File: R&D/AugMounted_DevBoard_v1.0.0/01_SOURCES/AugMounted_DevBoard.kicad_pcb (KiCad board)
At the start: 2 copper layers, 56.8 x 89.5 mm, 140 parts, among them J201 J_TYPE-C-31-M-13, J301 J_JST_S2B-PH-SM4-TB, J401 J_FH43BW-61S-0.2SHW, J501 J_0788641001_PAD, J502 J_0788641001, J503 J_0788641001, J504 J_0788641001_PAD, Q301 Q_BSS123WQ-7-F, Q302 Q_HSS2P10, Q303 Q_BSS123WQ-7-F, Q304 Q_BSS123WQ-7-F, Q305 Q_HSS2P10, Q401 Q_BSS123WQ-7-F, Q501 Q_BSS123WQ-7-F, SW501 SW_SKRTLAE010, SW601 SW_EC12D1564404, SW602 SW_SKRTLAE010, SW603 SW_SKRTLAE010, U201 ESP32-S3-WROOM-1U-N16R8, U202 U_MCP23017T-E/ML, U301 U_LP3987H-18B5F, U302 U_MAX17048G+T10, U303 U_BQ24296MRGER, U304 U_TPS63001DRCR, U305 U_TPS61087DRCR, U401 U_TXB0108PWR, U402 U_TXB0108PWR, U403 U_TXB0108PWR, U501 U_VCNL4040M3OE, U502 ICS‐41350, U503 LIS2DW12

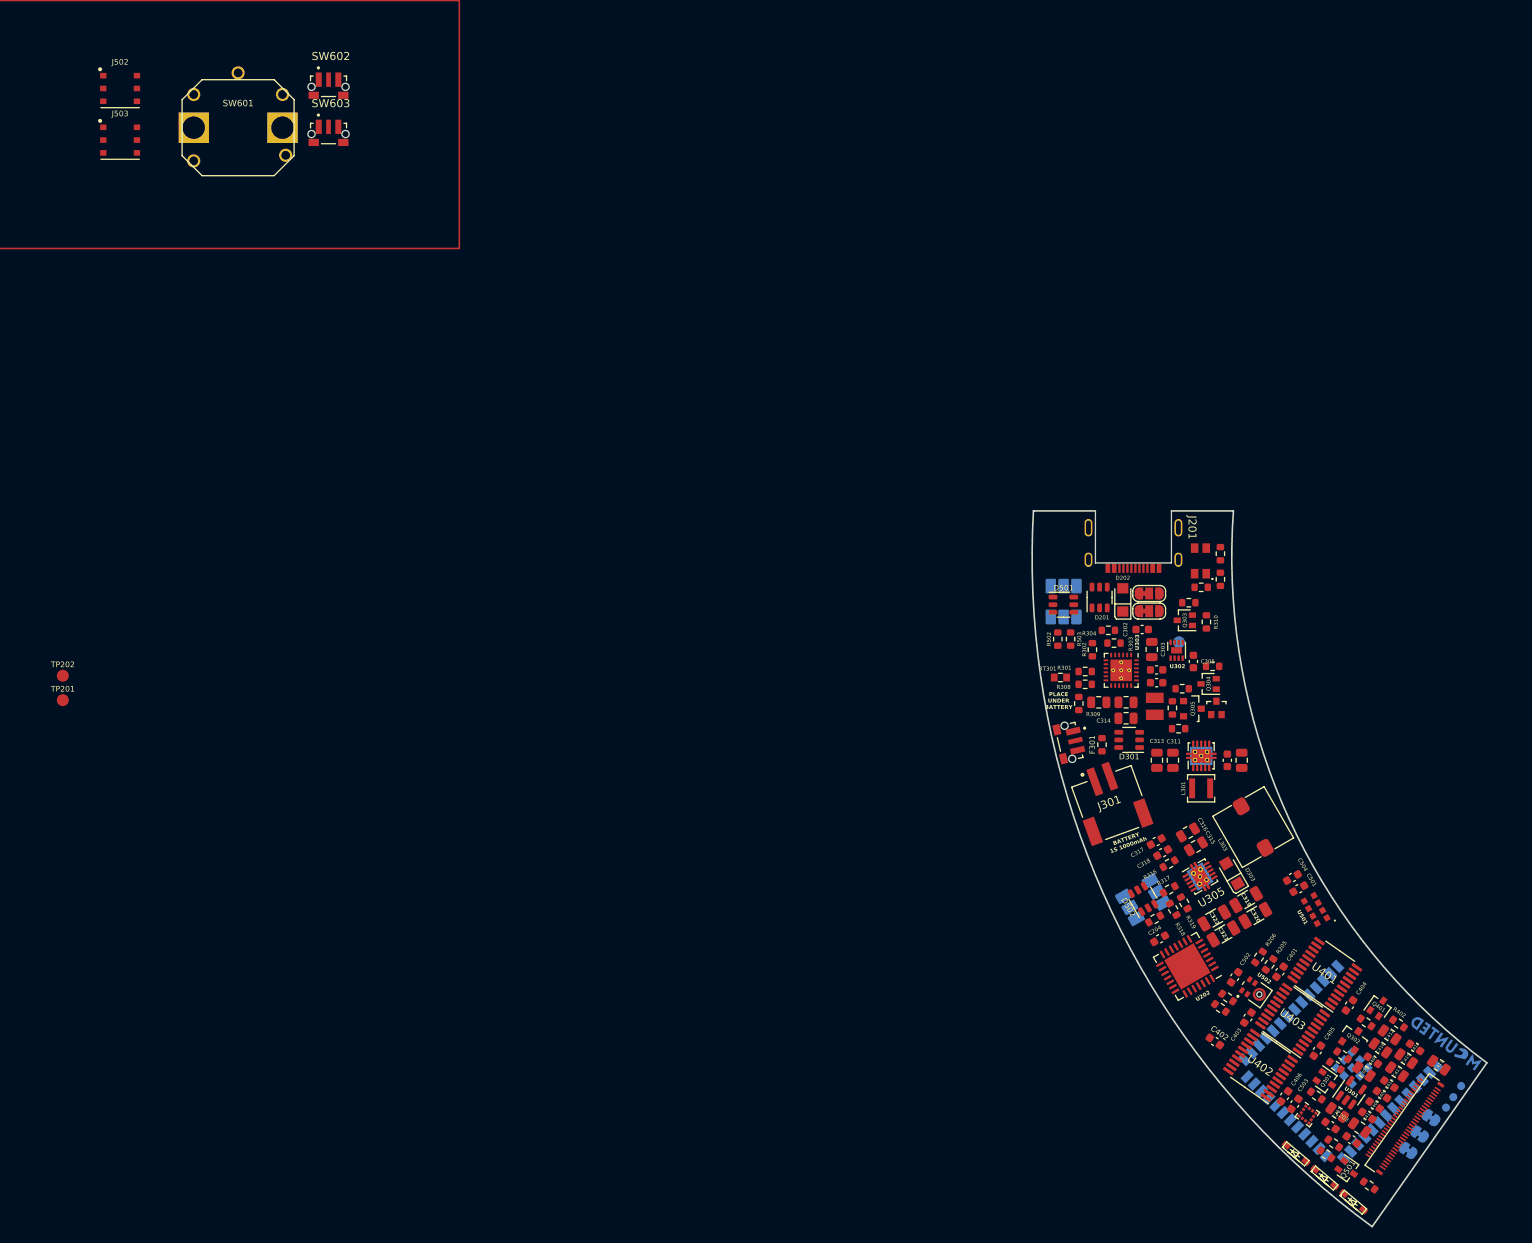
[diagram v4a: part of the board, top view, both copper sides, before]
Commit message: Added resistors for CC1 and CC2 pins, layout is started on the high part of the board
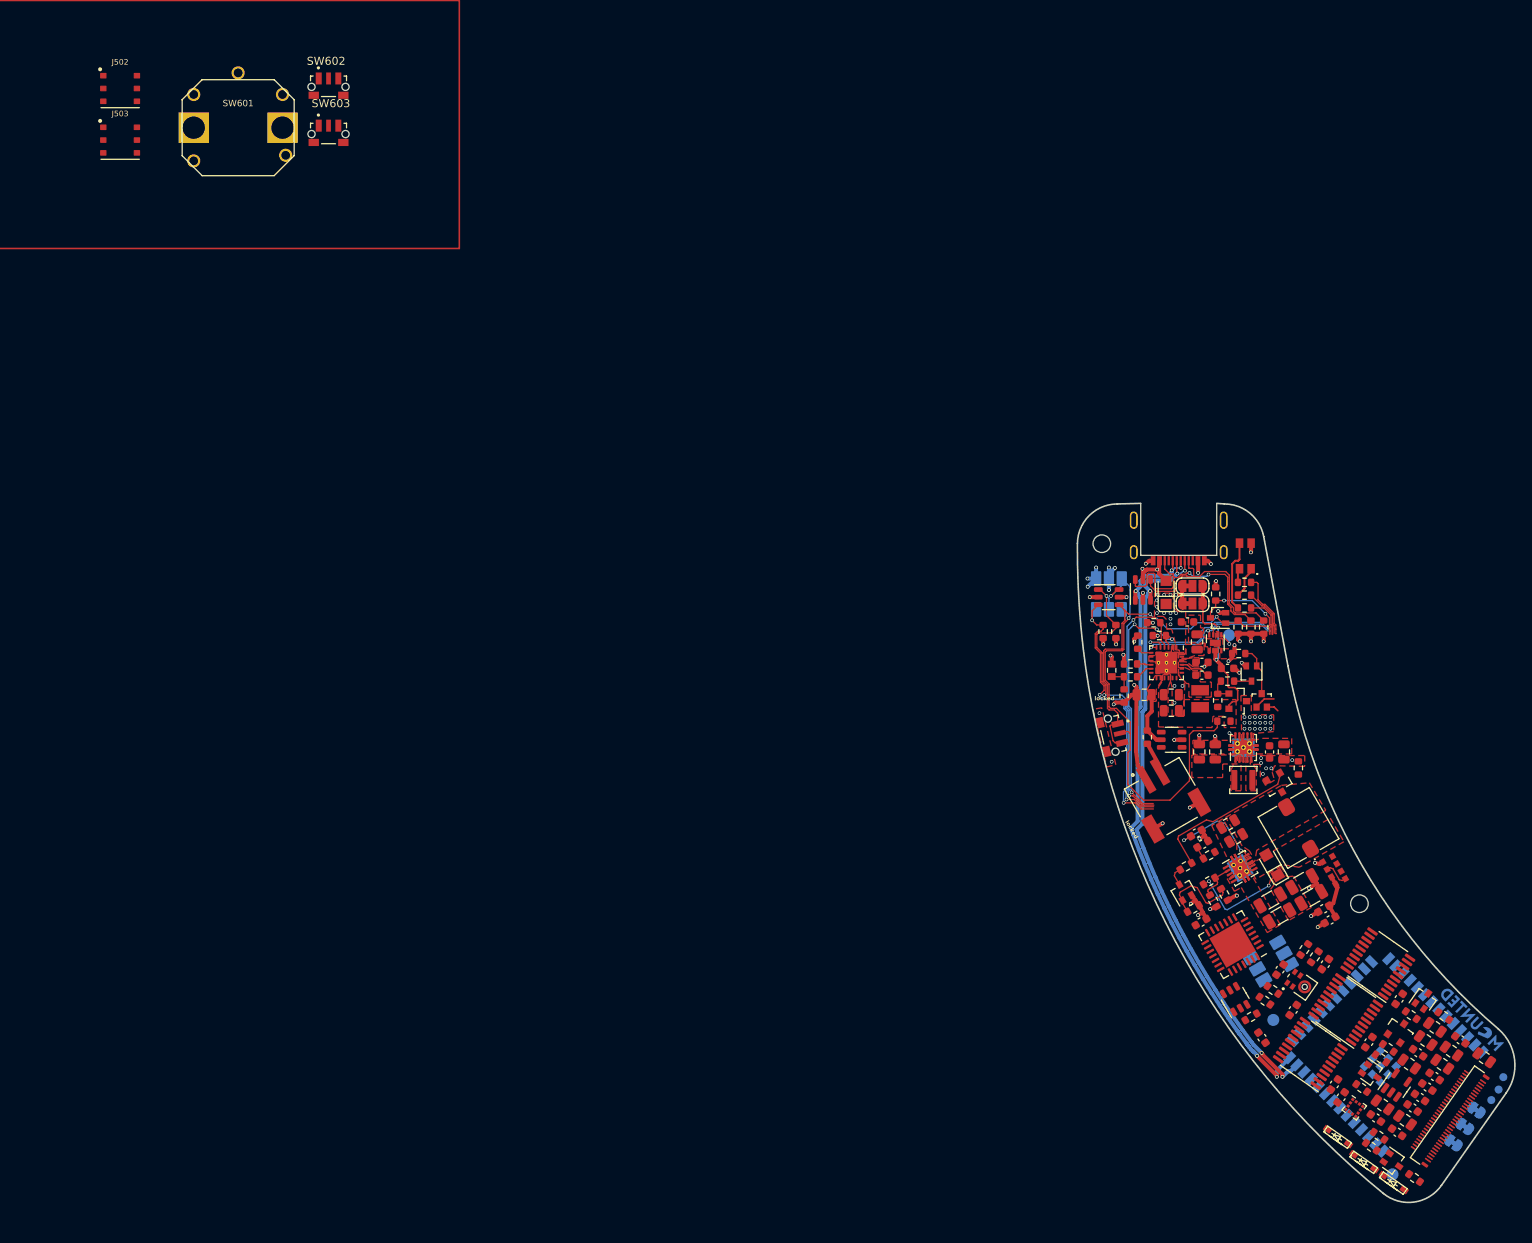
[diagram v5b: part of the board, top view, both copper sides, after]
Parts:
- added H101: MountingHole, MountingHole:MountingHole_2.2mm_M2, F.Cu at (342.3, 13.2)
- added H102: MountingHole, MountingHole:MountingHole_2.2mm_M2, F.Cu at (374.5, 58.2)
- added Q306: Q_BSS123WQ-7-F, .mounted-lib:SOT-323_SC-70_DIODES_INC, F.Cu at (352.5, 56.6)
- added Q307: Q_HSS2P10, .mounted-lib:SOT-23-3_HUASHUO, F.Cu at (364.3, 43.3)
- added R207: R_0603_5.23k_1%_0.1W, .mounted-lib:R_0603_1608Metric, F.Cu at (362.6, 23.6)
- added R208: R_0603_5.23k_1%_0.1W, .mounted-lib:R_0603_1608Metric, F.Cu at (361.0, 23.6)
- added R320: R_0603_1M_1%_0.1W, .mounted-lib:R_0603_1608Metric, F.Cu at (353.8, 58.8)
- added R321: R_0603_100k_1%_0.1W, .mounted-lib:R_0603_1608Metric, F.Cu at (366.9, 41.2)
- added R322: R_0603_0R_1%_0.1W, .mounted-lib:R_0603_1608Metric, F.Cu at (352.9, 53.5)
- TP201, TP202: moved to B.Cu
- moved TP201 176.5 mm to (378.7, 92.0), turned to 180 degrees
- moved TP202 157.3 mm to (363.8, 72.7), turned to 180 degrees
- moved J501 17.7 mm to (363.5, 65.4)
- moved R501 17.2 mm to (361.0, 72.3)
- moved D502 17.0 mm to (359.0, 70.1)
- moved R203 7.42 mm to (360.2, 21.2), turned to 0 degrees
- moved C321 7.36 mm to (364.5, 59.7)
- moved C320 7.36 mm to (368.5, 57.4)
- moved C322 7.36 mm to (363.4, 57.7)
- moved C319 7.36 mm to (367.4, 55.4)
- moved J301 6.87 mm to (350.3, 44.9), turned to 30 degrees
- moved U403 6.75 mm to (372.8, 71.4)
- moved U401 6.75 mm to (376.8, 65.7)
- moved C405 6.53 mm to (375.7, 75.5)
- moved RT301 6.48 mm to (343.6, 29.0), turned to 90 degrees
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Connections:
- net Net-(C308-Pad1) renamed /Battery Management/NET_BEFORE_INDUCTOR
- net Net-(J301-+) renamed /Battery Management/VBAT_NOT_FUSED
- net Net-(U303-PMID) renamed /Battery Management/PMID
- C315 pad 1: /Battery Management/VSYS -> /Battery Management/VSYS_CONTROLED_10V
- C316 pad 1: /Battery Management/VSYS -> /Battery Management/VSYS_CONTROLED_10V
- J201 pad A5: unconnected-(J201-CC1-PadA5) -> /MCU/CC1
- J201 pad B5: unconnected-(J201-CC2-PadB5) -> /MCU/CC2
- L303 pad 1: /Battery Management/VSYS -> /Battery Management/VSYS_CONTROLED_10V
- SJ301 pad 2: Net-(SJ301-C) -> GND
- SJ302 pad 2: Net-(SJ302-C) -> GND
- U303 pad 15: /Battery Management/VSYS -> /Battery Management/VSYS_UNCUT
- U303 pad 16: /Battery Management/VSYS -> /Battery Management/VSYS_UNCUT
- U303 pad 2: Net-(SJ302-C) -> GND
- U303 pad 8: Net-(SJ301-C) -> GND
- U305 pad 3: /Battery Management/10V_ENABLE -> /Battery Management/VSYS_CONTROLED_10V
- U305 pad 8: /Battery Management/VSYS -> /Battery Management/VSYS_CONTROLED_10V
- U305 pad 9: /Battery Management/VSYS -> /Battery Management/VSYS_CONTROLED_10V
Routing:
- net /MCU/USB_D+: track 0.00 -> 80.4 mm, vias 0 -> 5
- net /MCU/USB_D-: track 0.00 -> 80.1 mm, vias 0 -> 5
- net GND: track 0.00 -> 66.2 mm, vias 0 -> 41
- net /ENCODER_S1: track 0.00 -> 56.2 mm, vias 0 -> 2
- net /ENCODER_S2: track 0.00 -> 48.6 mm, vias 0 -> 2
- net /ENCODER_A: track 0.00 -> 38.0 mm, vias 0 -> 3
- net /ENCODER_B: track 0.00 -> 36.1 mm, vias 0 -> 3
- net /Battery Management/CHARGE_STATUS: track 0.00 -> 33.3 mm, vias 0 -> 2
- net /Battery Management/PGOOD: track 0.00 -> 32.9 mm, vias 0 -> 4
- net /MCU/CC2: track 0.00 -> 27.8 mm, vias 0 -> 2
- net /MCU/CC1: track 0.00 -> 24.3 mm
- net /Battery Management/VSYS_UNCUT: track 0.00 -> 20.5 mm, vias 0 -> 2
- net /SCL: track 0.00 -> 19.9 mm, vias 0 -> 2
- net Net-(Q307-G): track 0.00 -> 19.6 mm
- net /SDA: track 0.00 -> 18.1 mm, vias 0 -> 2
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- added copper zone on F.Cu, net +10V
- added copper zone on F.Cu, net +3.3V
- added copper zone on In2.Cu, net +3.3V
- added copper zone on F.Cu, net /Battery Management/NET_BEFORE_INDUCTOR
- added copper zone on F.Cu, net /Battery Management/PMID
- added copper zone on F.Cu, net /Battery Management/VBAT
- added copper zone on F.Cu, net /Battery Management/VSYS
- added copper zone on In2.Cu, net /Battery Management/VSYS
- added copper zone on F.Cu, net /Battery Management/VSYS_CONTROLED_10V
- added copper zone on F.Cu, net /Battery Management/VSYS_UNCUT
- added copper zone on In2.Cu, net /MCU/VBUS_USB
- added copper zone on F.Cu, net GND
- added copper zone on In1.Cu, net GND
- added copper zone on F.Cu, net Net-(D303-A)
- added copper zone on F.Cu, net Net-(U303-REGN)
- added copper zone on F.Cu, net Net-(U304-L1)
- added copper zone on F.Cu, net Net-(U304-L2)
- added copper zone on F.Cu, net VBUS
- added copper zone on In2.Cu, net VBUS
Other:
- board size 56.8 x 89.5 mm -> 54.7 x 87.4 mm
- copper layers 2 -> 4
- board text added: "locked"
- board text removed: "BATTERY 1S 1000mAh"
- board text removed: "PLACE UNDER BATTERY"

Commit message: Changed layout + all passive to 0402
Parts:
- removed Q401: Q_BSS123WQ-7-F, .mounted-lib:SOT-323_SC-70_DIODES_INC
- removed the R316 at (355.8, 52.1)
- removed the R317 at (355.8, 55.4)
- removed the R318 at (356.3, 57.8)
- removed R401, R402: R_0603_100k_1%_0.1W, .mounted-lib:R_0603_1608Metric
- removed SJ301, SJ302: SOLDER_JUMPER_3PIN_NC, .mounted-lib:SOLDER_JUMPER_3PIN_NC
- removed TP301: TESTPOINT_1.5MM, .mounted-lib:TESTPOINT_1.5MM
- added R320: R_0402_200k_1%_0.06W, .mounted-lib:R_0402_1005Metric, F.Cu at (159.0, 73.3)
- added R321: R_0402_26.7k_1%_0.06W, .mounted-lib:R_0402_1005Metric, F.Cu at (158.2, 71.5)
- added R323: R_0402_0R_1%_0.06W, .mounted-lib:R_0402_1005Metric, F.Cu at (158.1, 42.9)
- added R324: R_0402_0R_1%_0.06W, .mounted-lib:R_0402_1005Metric, F.Cu at (163.5, 40.5)
- C201, C302: value C_0603_1uF_16V_X7R_10% -> C_0402_1uF_10V_X7R_10%; footprint .mounted-lib:C_0603_1608Metric -> .mounted-lib:C_0402_1005Metric
- C203, C204, C305, C307, C317, C401, C402, C403, C404, C405, C406, C407, C408, C409, C410, C413, C414, C502, C503, C504: footprint .mounted-lib:C_0603_1608Metric -> .mounted-lib:C_0402_1005Metric
- C308: value C_0603_47nF_100V_X7R_10% -> C_0402_47nF_50V_X7R_10%; footprint .mounted-lib:C_0603_1608Metric -> .mounted-lib:C_0402_1005Metric
- C315, C316, C411, C412, C415, C416, C417: value C_0805_1uF_100V_X7S_20% -> C_0402_1uF_10V_X7R_10%; footprint .mounted-lib:C_0805_1608Metric -> .mounted-lib:C_0402_1005Metric
- C318: value C_0603_1.2nF_100V_X7R_5% -> C_0402_1.2nF_50V_X7R_10%; footprint .mounted-lib:C_0603_1608Metric -> .mounted-lib:C_0402_1005Metric
- R201, R205, R206, R207, R208, R305, R502, R503: footprint .mounted-lib:R_0603_1608Metric -> .mounted-lib:R_0402_1005Metric
- R202: value R_0603_33R_1%_0.1W -> R_0402_33R_1%_0.06W; footprint .mounted-lib:R_0603_1608Metric -> .mounted-lib:R_0402_1005Metric
- R203, R204: value R_0603_56R_1%_0.1W -> R_0402_56R_1%_0.06W; footprint .mounted-lib:R_0603_1608Metric -> .mounted-lib:R_0402_1005Metric
- R301: value R_0603_316R_0.5%_0.1W -> R_0402_316R_1%_0.06W; footprint .mounted-lib:R_0603_1608Metric -> .mounted-lib:R_0402_1005Metric
- R302, R303, R304: value R_0603_10k_1%_0.1W -> R_0402_10k_1%_0.06W; footprint .mounted-lib:R_0603_1608Metric -> .mounted-lib:R_0402_1005Metric
- R306, R504, R505, R506: value R_0603_100k_1%_0.1W -> R_0402_100k_1%_0.06W; footprint .mounted-lib:R_0603_1608Metric -> .mounted-lib:R_0402_1005Metric
- R307, R501, R507: value R_0603_0R_1%_0.1W -> R_0402_0R_1%_0.06W; footprint .mounted-lib:R_0603_1608Metric -> .mounted-lib:R_0402_1005Metric
- R308: value R_0603_5.23k_1%_0.1W -> R_0402_5.23k_1%_0.06W; footprint .mounted-lib:R_0603_1608Metric -> .mounted-lib:R_0402_1005Metric
- R310: renamed from R320; footprint .mounted-lib:R_0603_1608Metric -> .mounted-lib:R_0402_1005Metric
- R311: renamed from R321; value R_0603_100k_1%_0.1W -> R_0402_100k_1%_0.06W; footprint .mounted-lib:R_0603_1608Metric -> .mounted-lib:R_0402_1005Metric
- R312: renamed from R322; value R_0603_0R_1%_0.1W -> R_0402_0R_1%_0.06W; footprint .mounted-lib:R_0603_1608Metric -> .mounted-lib:R_0402_1005Metric
- R313: renamed from R310; value R_0603_100k_1%_0.1W -> R_0402_100k_1%_0.06W; footprint .mounted-lib:R_0603_1608Metric -> .mounted-lib:R_0402_1005Metric
- R314: renamed from R311; value R_0603_100k_1%_0.1W -> R_0402_100k_1%_0.06W; footprint .mounted-lib:R_0603_1608Metric -> .mounted-lib:R_0402_1005Metric
- R315: renamed from R312; value R_0603_100k_1%_0.1W -> R_0402_100k_1%_0.06W; footprint .mounted-lib:R_0603_1608Metric -> .mounted-lib:R_0402_1005Metric
- R316: renamed from R313; footprint .mounted-lib:R_0603_1608Metric -> .mounted-lib:R_0402_1005Metric
- R317: renamed from R314; value R_0603_100k_1%_0.1W -> R_0402_100k_1%_0.06W; footprint .mounted-lib:R_0603_1608Metric -> .mounted-lib:R_0402_1005Metric
- R318: renamed from R315; value R_0603_0R_1%_0.1W -> R_0402_0R_1%_0.06W; footprint .mounted-lib:R_0603_1608Metric -> .mounted-lib:R_0402_1005Metric
- R319: value R_0603_1M_1%_0.1W -> R_0402_42.2k_1%_0.06W; footprint .mounted-lib:R_0603_1608Metric -> .mounted-lib:R_0402_1005Metric
- U401, U402, U403: value U_TXB0108PWR -> U_TXS0108E; footprint .mounted-lib:TSSOP-20_4.4x6.5mm_P0.65mm_TEXAS_INSTRUMENTS -> .mounted-lib:VQFN-20_TEXAS_INSTRUMENTS
- moved LOGO101 296.0 mm to (96.1, 26.7), turned to 80 degrees
- moved R203 212.4 mm to (148.4, 37.5), turned to -90 degrees
- moved LED201 211.8 mm to (149.4, 33.9)
- moved R204 211.7 mm to (149.4, 37.5), turned to -90 degrees
- moved R202 210.6 mm to (150.4, 37.5), turned to 90 degrees
- moved D302 208.5 mm to (154.2, 44.6), turned to -90 degrees
- moved Q306 208.4 mm to (153.6, 48.9)
- moved H101 207.6 mm to (136.9, 43.1)
- moved C320 207.2 mm to (162.2, 76.2), turned to -65 degrees
- moved R316 206.8 mm to (153.6, 46.7)
- moved R208 206.0 mm to (155.5, 37.7)
- moved R318 205.1 mm to (154.0, 51.1), turned to 180 degrees
- moved C321 204.7 mm to (160.2, 72.0), turned to 115 degrees
- moved R313 204.7 mm to (155.5, 41.2), turned to 90 degrees
- moved R314 204.5 mm to (153.0, 38.9), turned to 180 degrees
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- renumbered Q306 to Q303, Q307 to Q304, Q303 to Q305, Q304 to Q306, Q305 to Q307
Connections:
- C413 pad 1: /OLED/VDD2 -> +10V
- C414 pad 1: /OLED/VDD2 -> +10V
- J401 pad 3: /OLED/VDD2 -> +10V
- J401 pad 59: /OLED/VDD2 -> +10V
- R301 pad 1: GND -> Net-(U303-ILIM)
- R301 pad 2: Net-(U303-ILIM) -> GND
- R304 pad 1: /Battery Management/CHARGE_STATUS -> +3.3V
- R304 pad 2: +3.3V -> /Battery Management/CHARGE_STATUS
- R319 pad 1: /Battery Management/10V_ENABLE -> Net-(U305-COMP)
- R319 pad 2: GND -> Net-(C318-Pad1)
- U302 pad 5: Net-(U302-~{ALRT}) -> unconnected-(U302-~{ALRT}-Pad5)
- U303 pad 2: GND -> Net-(U303-PSEL)
- U303 pad 8: GND -> Net-(U303-OTG)
- U401 pad 14: unconnected-(U401-B6-Pad14) -> /MCU/RGB_LSB
- U401 pad 7: unconnected-(U401-A6-Pad7) -> /OLED/RGB_LSB_1.8V
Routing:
- net /MCU/USB_D+: track 80.4 -> 0.00 mm, vias 5 -> 1
- net /MCU/USB_D-: track 80.1 -> 0.00 mm, vias 5 -> 1
- net GND: track 66.2 -> 1.48 mm, vias 41 -> 0
- net /ENCODER_S1: track 56.2 -> 0.00 mm, vias 2 -> 0
- net /ENCODER_S2: track 48.6 -> 0.00 mm, vias 2 -> 0
- net /ENCODER_A: track 38.0 -> 0.00 mm, vias 3 -> 0
- net /ENCODER_B: track 36.1 -> 0.00 mm, vias 3 -> 0
- net /Battery Management/CHARGE_STATUS: track 33.3 -> 0.00 mm, vias 2 -> 0
- net /Battery Management/PGOOD: track 32.9 -> 0.00 mm, vias 4 -> 0
- net /MCU/CC2: track 27.8 -> 0.00 mm, vias 2 -> 0
- net /MCU/CC1: track 24.3 -> 0.00 mm
- net /Battery Management/VSYS_UNCUT: track 20.5 -> 0.00 mm, vias 2 -> 12
- net /SCL: track 19.9 -> 0.00 mm, vias 2 -> 0
- net Net-(Q304-G): track 19.6 -> 0.00 mm
- net /SDA: track 18.1 -> 0.00 mm, vias 2 -> 0
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- removed copper zone on F.Cu, net VBUS
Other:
- board size 54.7 x 87.4 mm -> 55.7 x 82.9 mm
- board text added: "BATTERY 1S 1000mAh"
- board text added: "PLACE UNDER BATTERY"
- board text removed: "locked"
